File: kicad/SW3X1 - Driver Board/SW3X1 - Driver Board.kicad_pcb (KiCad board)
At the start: 2 copper layers, 128.3 x 66 mm, 39 parts, among them J1 SERIAL (3v3), J2 PWR, J3 CONTROL, J4 Channel 1, J5 Channel 2, J6 Channel 3, J7 Channel 4, J8 CH_OUT, U1 TPS5430DDA, U2 Pico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

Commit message: finalize driver board
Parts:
- moved JP1 1.27 mm to (78.2, 64.8)
- moved D3 0.48 mm to (81.3, 109.2)
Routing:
- net VIN: track 49.5 -> 48.1 mm
- net Net-(J1-Pad3): track 6.23 -> 7.50 mm
- net Vdrive: track 32.4 -> 31.3 mm
- net GND: vias 17 -> 16
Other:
- board text added: "JLCJLCJLCJLC"
- board text added: "SW3X1 Rev 1"
- board text removed: "- Label Headers (Silkscreen) - Check SMD footprint 10mm vs ? mm"

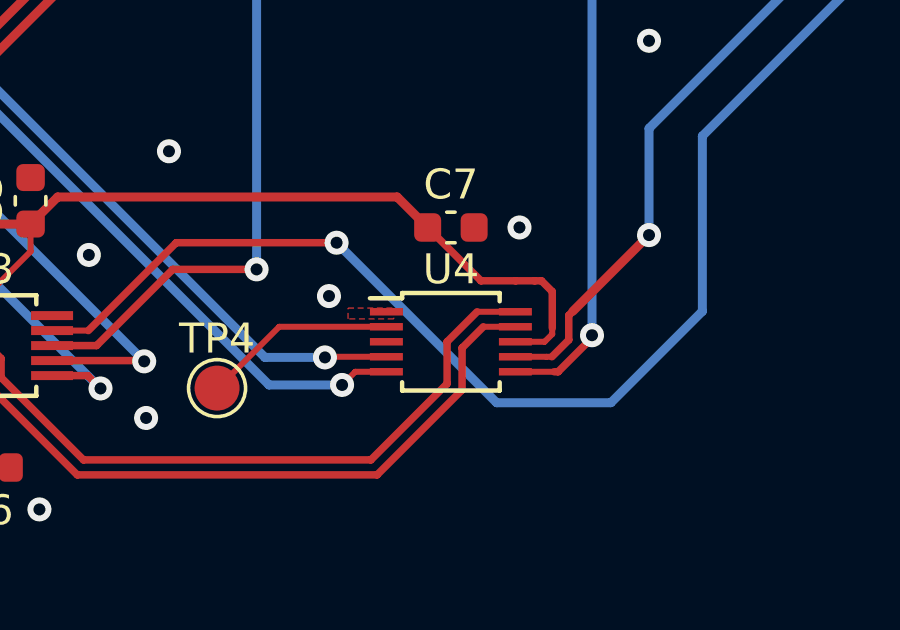
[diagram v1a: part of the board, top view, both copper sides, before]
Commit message: fix wrong ADC footprint
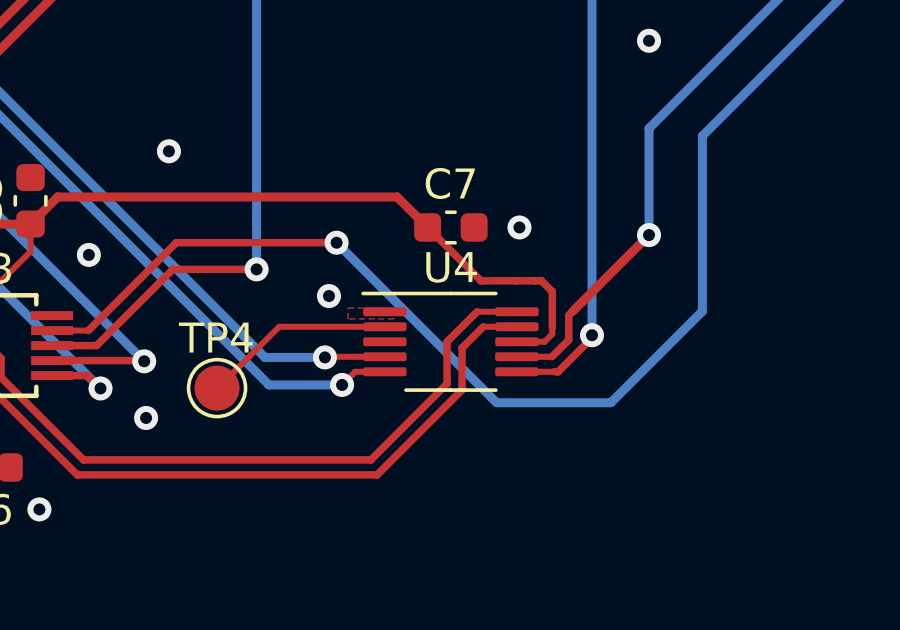
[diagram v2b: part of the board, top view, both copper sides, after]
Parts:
- U4: footprint Package_SO:TSSOP-10_3x3mm_P0.5mm -> Package_SO:VSSOP-10_3x3mm_P0.5mm
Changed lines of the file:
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@@
       (net 64 "Net-(TP4-Pad1)") (pinfunction "1") (pintype "passive"))
   )
-  (footprint "Package_SO:TSSOP-10_3x3mm_P0.5mm" locked (layer "F.Cu")
+  (footprint "Package_SO:VSSOP-10_3x3mm_P0.5mm" locked (layer "F.Cu")
     (at 148.336 90.424)
-    (descr "TSSOP10: plastic thin shrink small outline package; 10 leads; body width 3 mm; (see NXP SSOP-TSSOP-VSO-REFLOW.pdf and sot552-1_po.pdf)")
-    (tags "SSOP 0.5")
+    (descr "VSSOP, 10 Pin (http://www.ti.com/lit/ds/symlink/ads1115.pdf), generated with kicad-footprint-generator ipc_gullwing_generator.py")
+    (tags "VSSOP SO")
     (property "LCSC" "C193969")
     (property "MOUSER" "595-ADS1015IDGSR")
@@
     (property "Sheetfile" "SW3X1 - Driver Board.kicad_sch")
     (property "Sheetname" "")
-    (clearance 0.2)
-    (attr smd)
-    (fp_text reference "U4" (at 0 -2.413) (layer "F.SilkS")
-      (effects (font (size 1 1) (thickness 0.15)))
-    )
-    (fp_text value "ADS1015" (at 0 2.55) (layer "F.Fab")
+    (attr smd)
+    (fp_text reference "U4" (at 0 -2.45) (layer "F.SilkS")
+      (effects (font (size 1 1) (thickness 0.15)))
+    )
+    (fp_text value "ADS1015" (at 0 2.45) (layer "F.Fab")
       (effects (font (size 1 1) (thickness 0.15)))
     )
     (fp_text user "${REFERENCE}" (at 0 0) (layer "F.Fab")
-      (effects (font (size 0.6 0.6) (thickness 0.1)))
-    )
-    (fp_line (start -1.625 -1.45) (end -2.7 -1.45) (layer "F.SilkS") (width 0.15))
-    (fp_line (start 1.625 -1.625) (end 1.625 -1.35) (layer "F.SilkS") (width 0.15))
-    (fp_line (start -1.625 1.625) (end 1.625 1.625) (layer "F.SilkS") (width 0.15))
-    (fp_line (start 1.625 1.625) (end 1.625 1.35) (layer "F.SilkS") (width 0.15))
-    (fp_line (start -1.625 -1.625) (end -1.625 -1.45) (layer "F.SilkS") (width 0.15))
-    (fp_line (start -1.625 1.625) (end -1.625 1.35) (layer "F.SilkS") (width 0.15))
-    (fp_line (start -1.625 -1.625) (end 1.625 -1.625) (layer "F.SilkS") (width 0.15))
-    (fp_line (start -2.95 1.8) (end 2.95 1.8) (layer "F.CrtYd") (width 0.05))
-    (fp_line (start 2.95 -1.8) (end 2.95 1.8) (layer "F.CrtYd") (width 0.05))
-    (fp_line (start -2.95 -1.8) (end -2.95 1.8) (layer "F.CrtYd") (width 0.05))
-    (fp_line (start -2.95 -1.8) (end 2.95 -1.8) (layer "F.CrtYd") (width 0.05))
-    (fp_line (start -0.5 -1.5) (end 1.5 -1.5) (layer "F.Fab") (width 0.1))
-    (fp_line (start -1.5 -0.5) (end -0.5 -1.5) (layer "F.Fab") (width 0.1))
+      (effects (font (size 0.75 0.75) (thickness 0.11)))
+    )
+    (fp_line (start 0 1.61) (end -1.5 1.61) (layer "F.SilkS") (width 0.12))
+    (fp_line (start 0 -1.61) (end -2.925 -1.61) (layer "F.SilkS") (width 0.12))
+    (fp_line (start 0 1.61) (end 1.5 1.61) (layer "F.SilkS") (width 0.12))
+    (fp_line (start 0 -1.61) (end 1.5 -1.61) (layer "F.SilkS") (width 0.12))
+    (fp_line (start -3.18 1.75) (end 3.18 1.75) (layer "F.CrtYd") (width 0.05))
+    (fp_line (start 3.18 -1.75) (end -3.18 -1.75) (layer "F.CrtYd") (width 0.05))
+    (fp_line (start -3.18 -1.75) (end -3.18 1.75) (layer "F.CrtYd") (width 0.05))
+    (fp_line (start 3.18 1.75) (end 3.18 -1.75) (layer "F.CrtYd") (width 0.05))
+    (fp_line (start -0.75 -1.5) (end 1.5 -1.5) (layer "F.Fab") (width 0.1))
+    (fp_line (start 1.5 1.5) (end -1.5 1.5) (layer "F.Fab") (width 0.1))
+    (fp_line (start -1.5 1.5) (end -1.5 -0.75) (layer "F.Fab") (width 0.1))
+    (fp_line (start -1.5 -0.75) (end -0.75 -1.5) (layer "F.Fab") (width 0.1))
     (fp_line (start 1.5 -1.5) (end 1.5 1.5) (layer "F.Fab") (width 0.1))
-    (fp_line (start 1.5 1.5) (end -1.5 1.5) (layer "F.Fab") (width 0.1))
-    (fp_line (start -1.5 1.5) (end -1.5 -0.5) (layer "F.Fab") (width 0.1))
-    (pad "1" smd rect locked (at -2.15 -1) (size 1.1 0.25) (layers "F.Cu" "F.Paste" "F.Mask")
-      (net 2 "GND") (pinfunction "ADDR") (pintype "input"))
-    (pad "2" smd rect locked (at -2.15 -0.5) (size 1.1 0.25) (layers "F.Cu" "F.Paste" "F.Mask")
-      (net 64 "Net-(TP4-Pad1)") (pinfunction "ALERT/RDY") (pintype "output") (clearance 0.25))
-    (pad "3" smd rect locked (at -2.15 0) (size 1.1 0.25) (layers "F.Cu" "F.Paste" "F.Mask")
-      (net 2 "GND") (pinfunction "GND") (pintype "power_in"))
-    (pad "4" smd rect locked (at -2.15 0.5) (size 1.1 0.25) (layers "F.Cu" "F.Paste" "F.Mask")
-      (net 26 "/CH1_SENSE") (pinfunction "AIN0") (pintype "input"))
-    (pad "5" smd rect locked (at -2.15 1) (size 1.1 0.25) (layers "F.Cu" "F.Paste" "F.Mask")
-      (net 33 "/CH2_SENSE") (pinfunction "AIN1") (pintype "input"))
-    (pad "6" smd rect locked (at 2.15 1) (size 1.1 0.25) (layers "F.Cu" "F.Paste" "F.Mask")
-      (net 40 "/CH3_SENSE") (pinfunction "AIN2") (pintype "input"))
-    (pad "7" smd rect locked (at 2.15 0.5) (size 1.1 0.25) (layers "F.Cu" "F.Paste" "F.Mask")
-      (net 47 "/CH4_SENSE") (pinfunction "AIN3") (pintype "input"))
-    (pad "8" smd rect locked (at 2.15 0) (size 1.1 0.25) (layers "F.Cu" "F.Paste" "F.Mask")
-      (net 6 "+3.3V") (pinfunction "VDD") (pintype "power_in"))
-    (pad "9" smd rect locked (at 2.15 -0.5) (size 1.1 0.25) (layers "F.Cu" "F.Paste" "F.Mask")
-      (net 58 "/SDA_PER") (pinfunction "SDA") (pintype "bidirectional"))
-    (pad "10" smd rect locked (at 2.15 -1) (size 1.1 0.25) (layers "F.Cu" "F.Paste" "F.Mask")
-      (net 57 "/SCL_PER") (pinfunction "SCL") (pintype "input"))
-    (model "${KICAD6_3DMODEL_DIR}/Package_SO.3dshapes/TSSOP-10_3x3mm_P0.5mm.wrl"
+    (pad "1" smd roundrect locked (at -2.2 -1) (size 1.45 0.3) (layers "F.Cu" "F.Paste" "F.Mask") (roundrect_rratio 0.25)
+      (net 2 "GND") (pinfunction "ADDR") (pintype "input") (clearance 0.2))
+    (pad "2" smd roundrect locked (at -2.2 -0.5) (size 1.45 0.3) (layers "F.Cu" "F.Paste" "F.Mask") (roundrect_rratio 0.25)
+      (net 64 "Net-(TP4-Pad1)") (pinfunction "ALERT/RDY") (pintype "output") (clearance 0.2))
+    (pad "3" smd roundrect locked (at -2.2 0) (size 1.45 0.3) (layers "F.Cu" "F.Paste" "F.Mask") (roundrect_rratio 0.25)
+      (net 2 "GND") (pinfunction "GND") (pintype "power_in") (clearance 0.2))
+    (pad "4" smd roundrect locked (at -2.2 0.5) (size 1.45 0.3) (layers "F.Cu" "F.Paste" "F.Mask") (roundrect_rratio 0.25)
+      (net 26 "/CH1_SENSE") (pinfunction "AIN0") (pintype "input") (clearance 0.2))
+    (pad "5" smd roundrect locked (at -2.2 1) (size 1.45 0.3) (layers "F.Cu" "F.Paste" "F.Mask") (roundrect_rratio 0.25)
+      (net 33 "/CH2_SENSE") (pinfunction "AIN1") (pintype "input") (clearance 0.2))
+    (pad "6" smd roundrect locked (at 2.2 1) (size 1.45 0.3) (layers "F.Cu" "F.Paste" "F.Mask") (roundrect_rratio 0.25)
+      (net 40 "/CH3_SENSE") (pinfunction "AIN2") (pintype "input") (clearance 0.2))
+    (pad "7" smd roundrect locked (at 2.2 0.5) (size 1.45 0.3) (layers "F.Cu" "F.Paste" "F.Mask") (roundrect_rratio 0.25)
+      (net 47 "/CH4_SENSE") (pinfunction "AIN3") (pintype "input") (clearance 0.2))
+    (pad "8" smd roundrect locked (at 2.2 0) (size 1.45 0.3) (layers "F.Cu" "F.Paste" "F.Mask") (roundrect_rratio 0.25)
+      (net 6 "+3.3V") (pinfunction "VDD") (pintype "power_in") (clearance 0.2))
+    (pad "9" smd roundrect locked (at 2.2 -0.5) (size 1.45 0.3) (layers "F.Cu" "F.Paste" "F.Mask") (roundrect_rratio 0.25)
+      (net 58 "/SDA_PER") (pinfunction "SDA") (pintype "bidirectional") (clearance 0.2))
+    (pad "10" smd roundrect locked (at 2.2 -1) (size 1.45 0.3) (layers "F.Cu" "F.Paste" "F.Mask") (roundrect_rratio 0.25)
+      (net 57 "/SCL_PER") (pinfunction "SCL") (pintype "input") (clearance 0.2))
+    (model "${KICAD6_3DMODEL_DIR}/Package_SO.3dshapes/VSSOP-10_3x3mm_P0.5mm.wrl"
       (offset (xyz 0 0 0))
       (scale (xyz 1 1 1))
@@
     (property "Sheetfile" "SW3X1 - Driver Board.kicad_sch")
     (property "Sheetname" "")
-    (attr exclude_from_pos_files)
+    (property "exclude_from_bom" "")
+    (attr exclude_from_pos_files exclude_from_bom)
     (fp_text reference "JP1" (at 0 -1.8 90) (layer "F.SilkS")
       (effects (font (size 1 1) (thickness 0.15)))

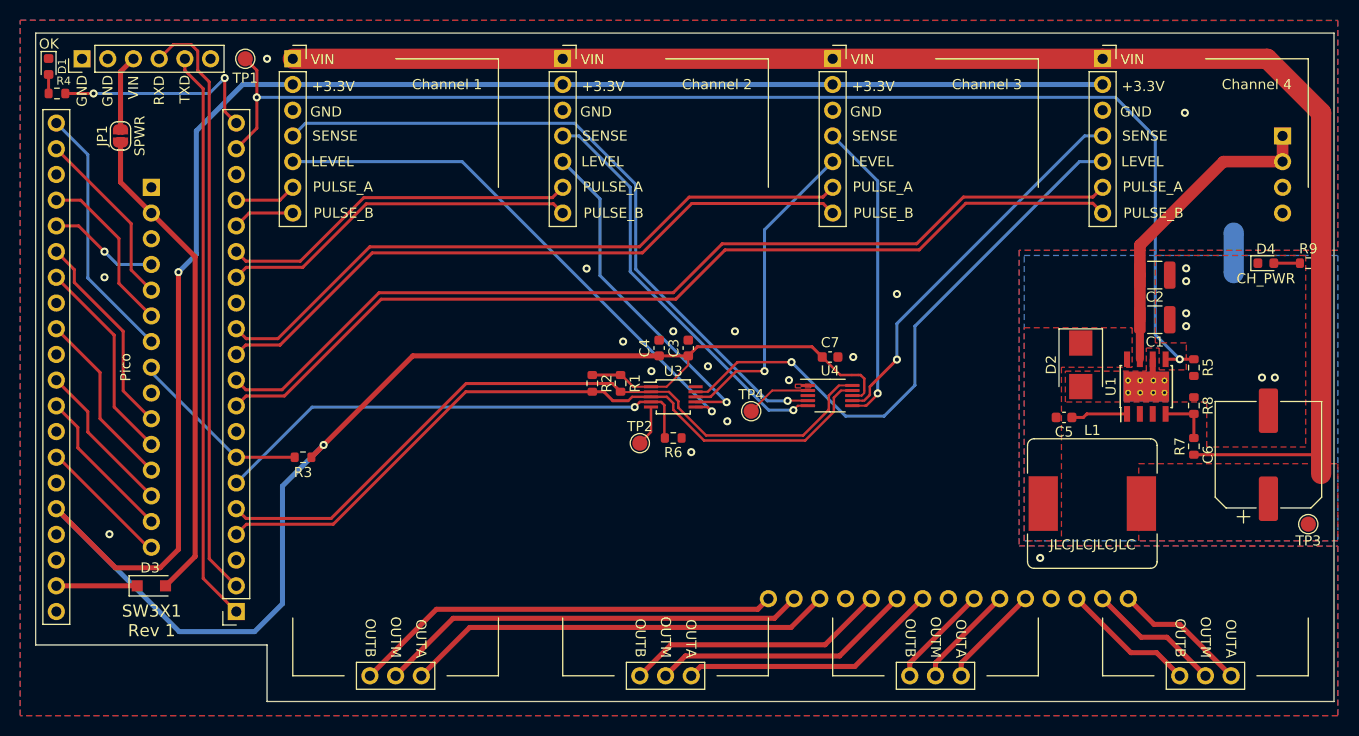
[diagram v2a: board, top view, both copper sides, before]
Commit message: align modules on the same 0.1" grid
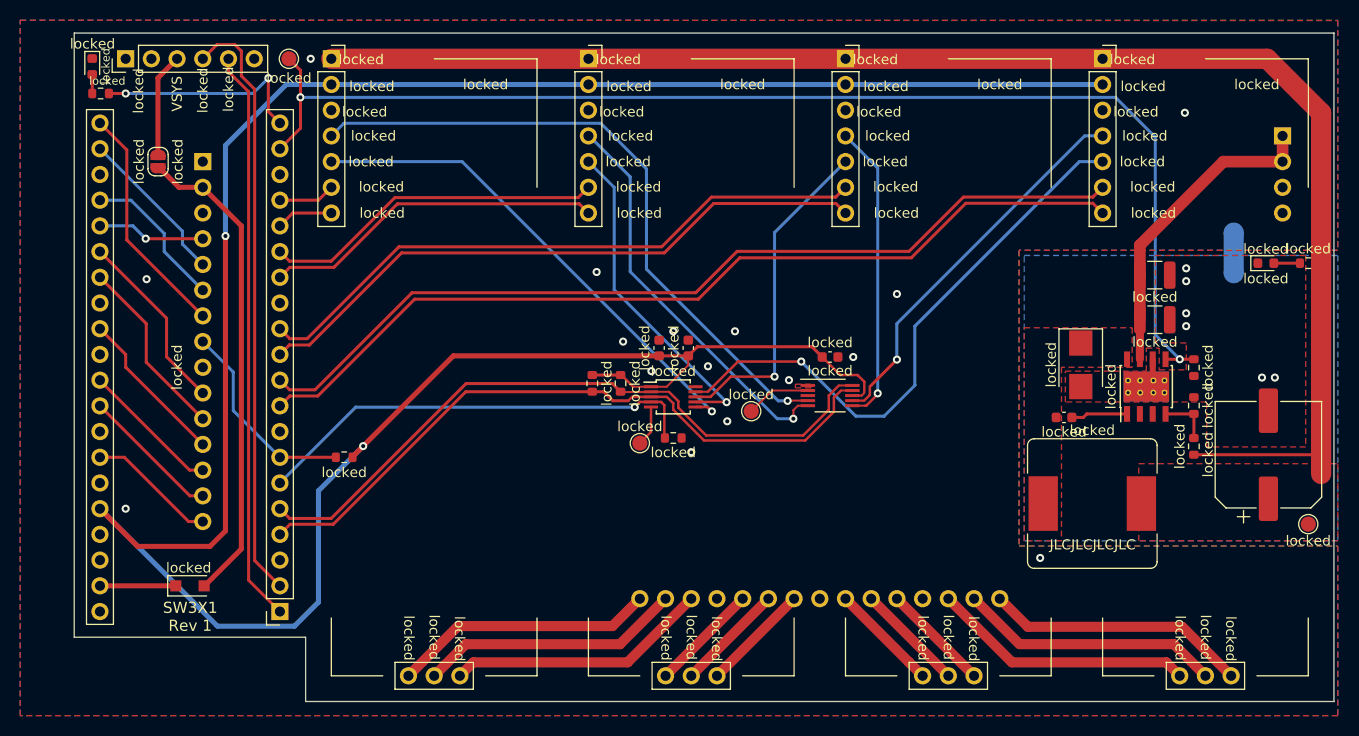
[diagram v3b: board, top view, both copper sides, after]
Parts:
- J4: value Channel 1 -> locked
- J5: value Channel 2 -> locked
- J6: value Channel 3 -> locked
- J7: value Channel 4 -> locked
- U2: value Pico -> locked
- locked: renamed from U3; value MCP4728 -> locked
- locked: renamed from R9; value 1.5K -> locked
- locked: renamed from L1; value 15uH -> locked
- locked: renamed from C2; value 10uF -> locked
- locked: renamed from JP1; value SPWR -> locked
- locked: renamed from R1; value 4.7K -> locked
- locked: renamed from TP2; value ~{BSY} -> locked
- locked: renamed from R4; value 1.5K -> locked
- locked: renamed from D1; value OK -> locked
- locked: renamed from TP3; value 9.2V -> locked
- locked: renamed from R2; value 4.7K -> locked
- locked: renamed from D2; value SSB44-E3 -> locked
- locked: renamed from R6; value 10K -> locked
- locked: renamed from R8; value 1.5K -> locked
- locked: renamed from R5; value 100K -> locked
- locked: renamed from C6; value 180uF -> locked
- locked: renamed from C5; value 10nF -> locked
- locked: renamed from D3; value DSS14 -> locked
- locked: renamed from D4; value CH_PWR -> locked
- locked: renamed from C3; value 10uF -> locked
- locked: renamed from R3; value 10K -> locked
- locked: renamed from C7; value 100nF -> locked
- locked: renamed from TP1; value EN -> locked
- locked: renamed from J8; value CH_OUT -> locked
- locked: renamed from TP4; value RDY -> locked
- locked: renamed from U4; value ADS1015 -> locked
- locked: renamed from R7; value 10K -> locked
- locked: renamed from U1; value TPS5430DDA -> locked
- locked: renamed from C4; value 100nF -> locked
- locked: renamed from C1; value 10uF -> locked
- moved locked 12.7 mm to (129.5, 110.5)
- moved locked 5.68 mm to (86.4, 67.3)
- moved locked 4.49 mm to (81.9, 67.3)
- moved U2 4.31 mm to (85.1, 87.6)
- moved locked 4.31 mm to (76.3, 60.6)
- moved locked 4.31 mm to (75.4, 57.9)
- moved locked 4.31 mm to (94.9, 57.1)
- moved locked 4.31 mm to (78.7, 57.1)
- moved locked 4.06 mm to (100.3, 96.5)
- moved J4 3.81 mm to (109.2, 87.6)
- moved locked 3.81 mm to (85.1, 109.2)
- moved J5 2.54 mm to (134.6, 87.6)
- moved J6 1.27 mm to (160.0, 87.6)
- renumbered J1 to locked, J3 to locked, J2 to locked
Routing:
- net Net-(J4-Pad10): track 42.5 -> 26.0 mm
- net Net-(J4-Pad9): track 42.5 -> 26.0 mm
- net Net-(J4-Pad8): track 42.5 -> 26.0 mm
- net Net-(J5-Pad10): track 26.0 -> 10.8 mm
- net Net-(J5-Pad9): track 26.0 -> 10.8 mm
- net Net-(J5-Pad8): track 26.0 -> 10.8 mm
- net Net-(J7-Pad8): track 13.3 -> 26.0 mm
- net Net-(J7-Pad9): track 13.3 -> 26.0 mm
- net Net-(J7-Pad10): track 13.3 -> 26.0 mm
- net +3.3V: track 269.5 -> 257.1 mm
- net /SCL_PER: track 72.0 -> 67.7 mm
- net /CH4_PA: track 94.3 -> 90.0 mm
- net /~{LDAC}: track 48.9 -> 44.6 mm
- net /CH4_PB: track 94.3 -> 90.0 mm
- net /SDA_PER: track 72.2 -> 67.9 mm
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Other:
- board size 128.3 x 66 mm -> 124.5 x 66 mm

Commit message: use ESP32
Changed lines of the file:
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@@
   (title_block
     (title "SW3X1 - Driver Board")
-    (date "2022-09-29")
+    (date "2022-11-04")
     (rev "1")
     (company "saawsm")
@@
     (fp_circle (center 0 0) (end 1.25 0) (layer "F.CrtYd") (width 0.05) (fill none))
     (pad "1" smd circle locked (at 0 0 180) (size 1.5 1.5) (layers "F.Cu" "F.Mask")
-      (net 5 "+9V") (pinfunction "1") (pintype "passive"))
+      (net 5 "+9V") (pinfunction "1") (pintype "passive") (thermal_width 0.5))
   )
   (footprint "Diode_SMD:D_SMB" locked (layer "F.Cu")
@@
     (fp_line (start -0.64944 -0.79908) (end -0.64944 0.80112) (layer "F.Fab") (width 0.1))
     (pad "1" smd rect locked (at -2.15 0 270) (size 2.5 2.3) (layers "F.Cu" "F.Paste" "F.Mask")
-      (net 4 "Net-(C5-Pad2)") (pinfunction "K") (pintype "passive"))
+      (net 4 "Net-(C5-Pad2)") (pinfunction "K") (pintype "passive") (thermal_width 1))
     (pad "2" smd rect locked (at 2.15 0 270) (size 2.5 2.3) (layers "F.Cu" "F.Paste" "F.Mask")
       (net 74 "GND1") (pinfunction "A") (pintype "passive") (thermal_width 2))
@@
       (net 5 "+9V") (pintype "passive"))
     (pad "2" smd roundrect locked (at 4.35 0 90) (size 4.4 1.9) (layers "F.Cu" "F.Paste" "F.Mask") (roundrect_rratio 0.1315789474)
-      (net 74 "GND1") (pintype "passive"))
+      (net 74 "GND1") (pintype "passive") (thermal_width 1))
     (model "${KICAD6_3DMODEL_DIR}/Capacitor_SMD.3dshapes/CP_Elec_10x7.9.wrl"
       (offset (xyz 0 0 0))
@@
   (segment locked (start 149.86 64.77) (end 153.039586 67.949586) (width 0.3) (layer "B.Cu") (net 40))
   (segment locked (start 135.042 90.551) (end 136.525 90.551) (width 0.25) (layer "F.Cu") (net 41))
-  (segment locked (start 142.810698 88.553105) (end 142.84978 88.553105) (width 0.25) (layer "F.Cu") (net 41))
   (segment locked (start 138.522895 88.553105) (end 142.84978 88.553105) (width 0.25) (layer "F.Cu") (net 41))
   (segment locked (start 136.525 90.551) (end 138.522895 88.553105) (width 0.25) (layer "F.Cu") (net 41))
@@
     (connect_pads (clearance 0.3))
     (min_thickness 0.3) (filled_areas_thickness no)
-    (fill yes (thermal_gap 0.5) (thermal_bridge_width 0.5))
+    (fill yes (thermal_gap 0.5) (thermal_bridge_width 1))
     (polygon
       (pts

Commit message: misc. cleanup
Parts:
- removed the locked at (195.6, 77.3)
- added R9: 4.7K, Resistor_SMD:R_0603_1608Metric, F.Cu at (195.6, 77.3)
- locked: value CONTROL -> locked
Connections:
- locked pad 2: Vdrive -> VIN (x3)
- locked pad 1: VIN -> VDD
- locked pad 2: VIN -> VDD (x2)
- locked pad 1: Vdrive -> VIN
- locked pad 7: Vdrive -> VIN
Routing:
- net VDD: track 0.00 -> 47.7 mm
- net Vdrive: track 31.3 -> 0.00 mm
- net VIN: track 47.7 -> 31.3 mm
